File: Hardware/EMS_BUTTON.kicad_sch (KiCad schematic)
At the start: 6 parts, among them J23 WAFER-GH1.25-4PWB, U52 TLP2362

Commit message: 修存档拉线
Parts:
- renumbered C126 to C141, R40 to R131, R102 to R132, R58 to R133, U52 to U54

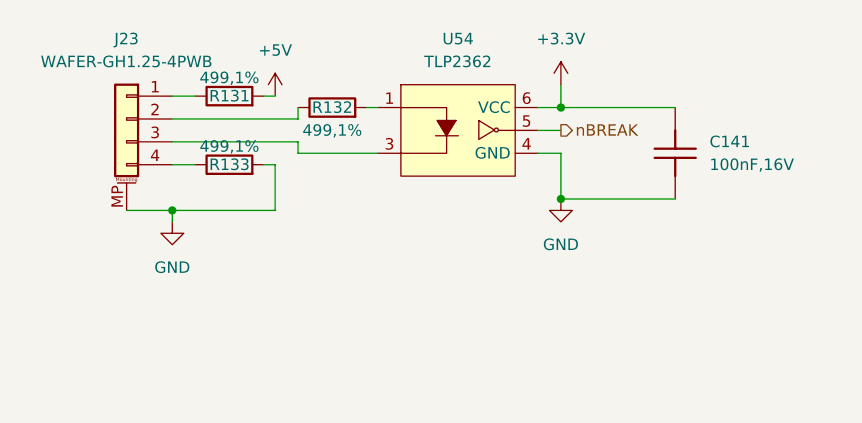
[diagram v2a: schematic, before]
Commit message: 修改PCB，上传py32抱闸驱动代码，上传HPM board
调整抱闸驱动栅极电阻
急停光耦增加上拉电阻和滤波电路
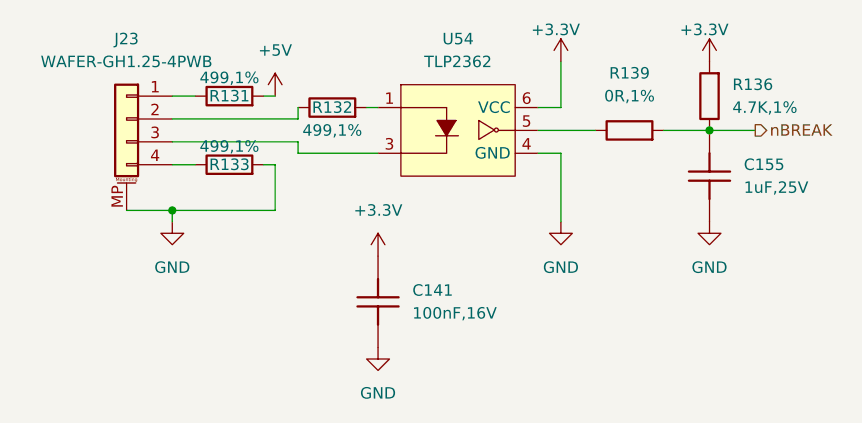
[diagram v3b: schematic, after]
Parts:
- added C155: 1uF,25V, Capacitor_SMD:C_0402_1005Metric, symbol HPM6280Foc:CL05A105KA5NQNC
- added R136: 4.7K,1%, Resistor_SMD:R_0402_1005Metric, symbol HPM6280Foc:0402WGF4701TCE
- added R139: 0R,1%, Resistor_SMD:R_0402_1005Metric, symbol HPM6280Foc:0402WGF0000TCE
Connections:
- net +3.3V: now also R136.2
- net GND: now also C155.2
- net nBREAK: now also C155.1, R136.1, R139.2; no longer U54.5
- new net: R139.1, U54.5
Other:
- moved on the sheet: C141
